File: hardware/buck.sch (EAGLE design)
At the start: 11 parts, among them X1 MOLEX_4HORIZONTAL

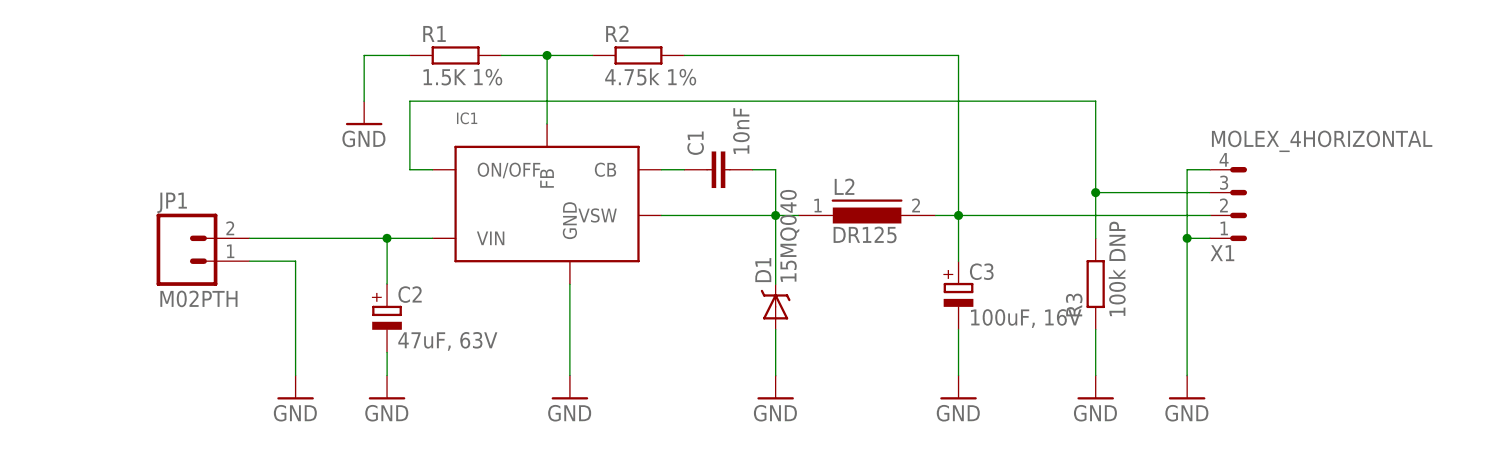
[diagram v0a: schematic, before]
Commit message: move silkscreen labels
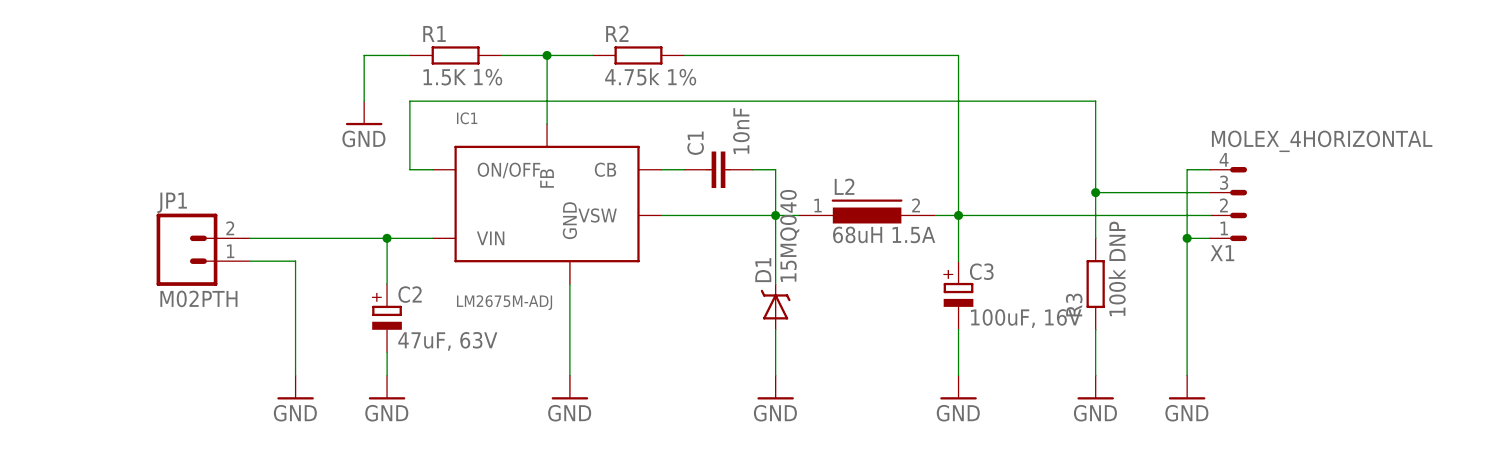
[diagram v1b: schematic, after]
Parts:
- IC1: value (none) -> LM2675M-ADJ
- L2: value DR125 -> 68uH 1.5A
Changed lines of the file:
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@@
 </classes>
 <parts>
-<part name="IC1" library="Simplex-ICs" deviceset="LM2674" device=""/>
+<part name="IC1" library="Simplex-ICs" deviceset="LM2674" device="" value="LM2675M-ADJ"/>
 <part name="GND1" library="supply1" deviceset="GND" device=""/>
 <part name="R1" library="rcl" deviceset="R-EU_" device="R0805W" value="1.5K 1%"/>
@@
 <part name="C3" library="rcl" deviceset="CPOL-EU" device="D" value="100uF, 16V"/>
 <part name="GND7" library="supply1" deviceset="GND" device=""/>
-<part name="L2" library="inductors" deviceset="DR125" device=""/>
+<part name="L2" library="inductors" deviceset="DR125" device="" value="68uH 1.5A"/>
 <part name="JP1" library="SparkFun-Connectors" deviceset="M02" device="PTH"/>
 <part name="X1" library="Simplex-Connectors" deviceset="MOLEX_4" device="HORIZONTAL"/>

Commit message: latest
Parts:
- removed R3: 100k DNP, rcl:R-EU_R0805W
- removed X1: MOLEX_4HORIZONTAL, Simplex-Connectors:MOLEX_4HORIZONTAL
- added X2: MKDSN1,5/4-5,08, con-phoenix-508:MKDSN1,5/4-5,08
- JP1: value M02PTH -> M01PTH; device SparkFun-Connectors:M02PTH -> SparkFun-Connectors:M01PTH
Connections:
- net GND: now also X2-2.KL, X2-3.KL; no longer JP1.1, R3.1, X1.1, X1.4
- net N$4: now also X2-4.KL; no longer X1.3
- net N$5: now also JP1.1; no longer R3.2, X1.2
- net N$6: now also X2-1.KL; no longer JP1.2
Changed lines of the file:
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@@
 <part name="GND7" library="supply1" deviceset="GND" device=""/>
 <part name="L2" library="inductors" deviceset="DR125" device="" value="68uH 1.5A"/>
-<part name="JP1" library="SparkFun-Connectors" deviceset="M02" device="PTH"/>
-<part name="X1" library="Simplex-Connectors" deviceset="MOLEX_4" device="HORIZONTAL"/>
-<part name="R3" library="rcl" deviceset="R-EU_" device="R0805W" value="100k DNP"/>
-<part name="GND8" library="supply1" deviceset="GND" device=""/>
+<part name="X2" library="con-phoenix-508" deviceset="MKDSN1,5/4-5,08" device=""/>
+<part name="JP1" library="SparkFun-Connectors" deviceset="M01" device="PTH"/>
 </parts>
 <sheets>
@@
 <instance part="GND7" gate="1" x="160.02" y="45.72"/>
 <instance part="L2" gate="G$1" x="149.86" y="66.04"/>
-<instance part="JP1" gate="G$1" x="73.66" y="60.96"/>
-<instance part="X1" gate="G$1" x="190.5" y="68.58"/>
-<instance part="R3" gate="G$1" x="175.26" y="58.42" rot="R90"/>
-<instance part="GND8" gate="1" x="175.26" y="45.72"/>
+<instance part="X2" gate="-1" x="78.74" y="63.5" rot="R180"/>
+<instance part="X2" gate="-2" x="78.74" y="60.96" rot="R180"/>
+<instance part="X2" gate="-3" x="190.5" y="63.5"/>
+<instance part="X2" gate="-4" x="190.5" y="66.04"/>
+<instance part="JP1" gate="G$1" x="193.04" y="78.74" rot="R180"/>
 </instances>
 <busses>
@@
 <wire x1="81.28" y1="60.96" x2="86.36" y2="60.96" width="0.1524" layer="91"/>
 <wire x1="86.36" y1="60.96" x2="86.36" y2="48.26" width="0.1524" layer="91"/>
-<pinref part="JP1" gate="G$1" pin="1"/>
+<pinref part="X2" gate="-2" pin="KL"/>
 </segment>
 <segment>
@@
 <wire x1="185.42" y1="63.5" x2="185.42" y2="48.26" width="0.1524" layer="91"/>
 <pinref part="GND5" gate="1" pin="GND"/>
-<pinref part="X1" gate="G$1" pin="4"/>
-<wire x1="185.42" y1="63.5" x2="185.42" y2="71.12" width="0.1524" layer="91"/>
-<pinref part="X1" gate="G$1" pin="1"/>
-<wire x1="185.42" y1="71.12" x2="187.96" y2="71.12" width="0.1524" layer="91"/>
-<junction x="185.42" y="63.5"/>
+<pinref part="X2" gate="-3" pin="KL"/>
 </segment>
 <segment>
@@
 <pinref part="GND7" gate="1" pin="GND"/>
 <wire x1="160.02" y1="53.34" x2="160.02" y2="48.26" width="0.1524" layer="91"/>
-</segment>
-<segment>
-<pinref part="R3" gate="G$1" pin="1"/>
-<pinref part="GND8" gate="1" pin="GND"/>
-<wire x1="175.26" y1="53.34" x2="175.26" y2="48.26" width="0.1524" layer="91"/>
 </segment>
 </net>
@@
 <wire x1="160.02" y1="60.96" x2="160.02" y2="66.04" width="0.1524" layer="91"/>
 <pinref part="L2" gate="G$1" pin="2"/>
-<pinref part="X1" gate="G$1" pin="3"/>
+<pinref part="X2" gate="-4" pin="KL"/>
 </segment>
 </net>
@@
 <wire x1="96.52" y1="58.42" x2="96.52" y2="63.5" width="0.1524" layer="91"/>
 <junction x="96.52" y="63.5"/>
-<pinref part="JP1" gate="G$1" pin="2"/>
+<pinref part="X2" gate="-1" pin="KL"/>
 </segment>
 </net>
@@
 <wire x1="101.6" y1="71.12" x2="99.06" y2="71.12" width="0.1524" layer="91"/>
 <wire x1="99.06" y1="71.12" x2="99.06" y2="78.74" width="0.1524" layer="91"/>
-<wire x1="99.06" y1="78.74" x2="175.26" y2="78.74" width="0.1524" layer="91"/>
-<wire x1="175.26" y1="78.74" x2="175.26" y2="68.58" width="0.1524" layer="91"/>
-<pinref part="X1" gate="G$1" pin="2"/>
-<wire x1="175.26" y1="68.58" x2="187.96" y2="68.58" width="0.1524" layer="91"/>
-<pinref part="R3" gate="G$1" pin="2"/>
-<wire x1="175.26" y1="63.5" x2="175.26" y2="68.58" width="0.1524" layer="91"/>
-<junction x="175.26" y="68.58"/>
+<wire x1="99.06" y1="78.74" x2="185.42" y2="78.74" width="0.1524" layer="91"/>
+<pinref part="JP1" gate="G$1" pin="1"/>
 </segment>
 </net>
